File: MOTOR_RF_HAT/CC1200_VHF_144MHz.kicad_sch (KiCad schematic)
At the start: 41 parts, among them J1 SMA, U1 CC1200RHBR, Y1 40MHz

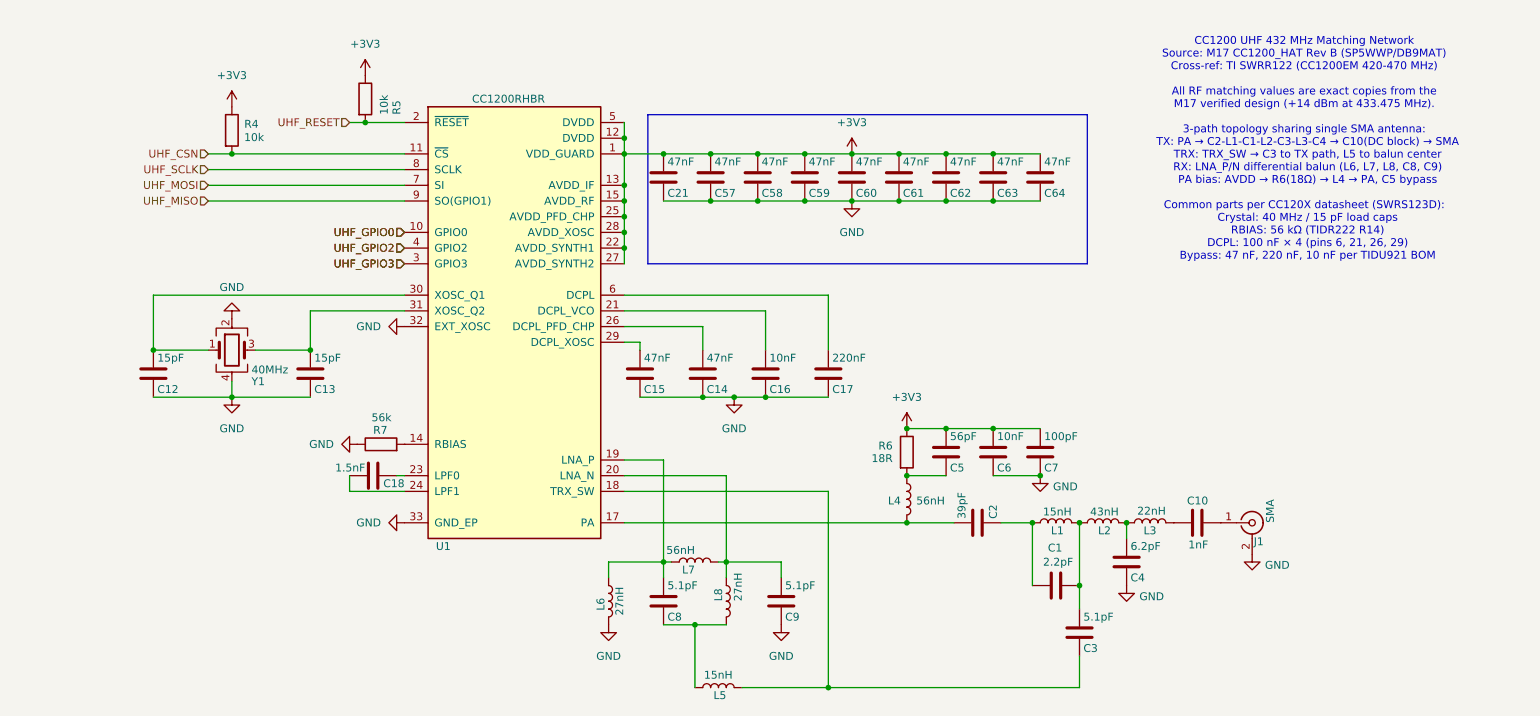
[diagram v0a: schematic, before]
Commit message: MOTOR_RF_HAT: port full RF_HAT project with all libs localized
Copied complete RF_HAT_out KiCad project (schematic + PCB layout +
4 hierarchical sub-sheets) as the base for the combined board.

Changes from original RF_HAT:
- Renamed RF_HAT → MOTOR_RF_HAT in all project/schematic references
- Imported LMR51420YDDCR + XRTC303020D4R7MBCA symbols from personal
  lib into project-local components.kicad_sym
- Copied corresponding footprints + 3D models (SOT-23-6, inductor)
  into components.pretty/ and components.3dshapes/
- Fixed all lib: → components: references in schematics and PCB
- Removed reference/ directory (schematics are now live sub-sheets)
- ERC: 20 violations (19 pre-existing from RF_HAT + 1 from rename)
- Zero external library dependencies — fully self-contained

Ready to add motor driver (A4950E), encoder, and IMU (ADXL345)
sub-sheets. Existing CC1200 UHF/VHF, Pi header, Pico, power,
NeoPixel, and buzzer circuits carry over unchanged.

Co-Authored-By: Claude Opus 4.6 (1M context) <noreply@anthropic.com>
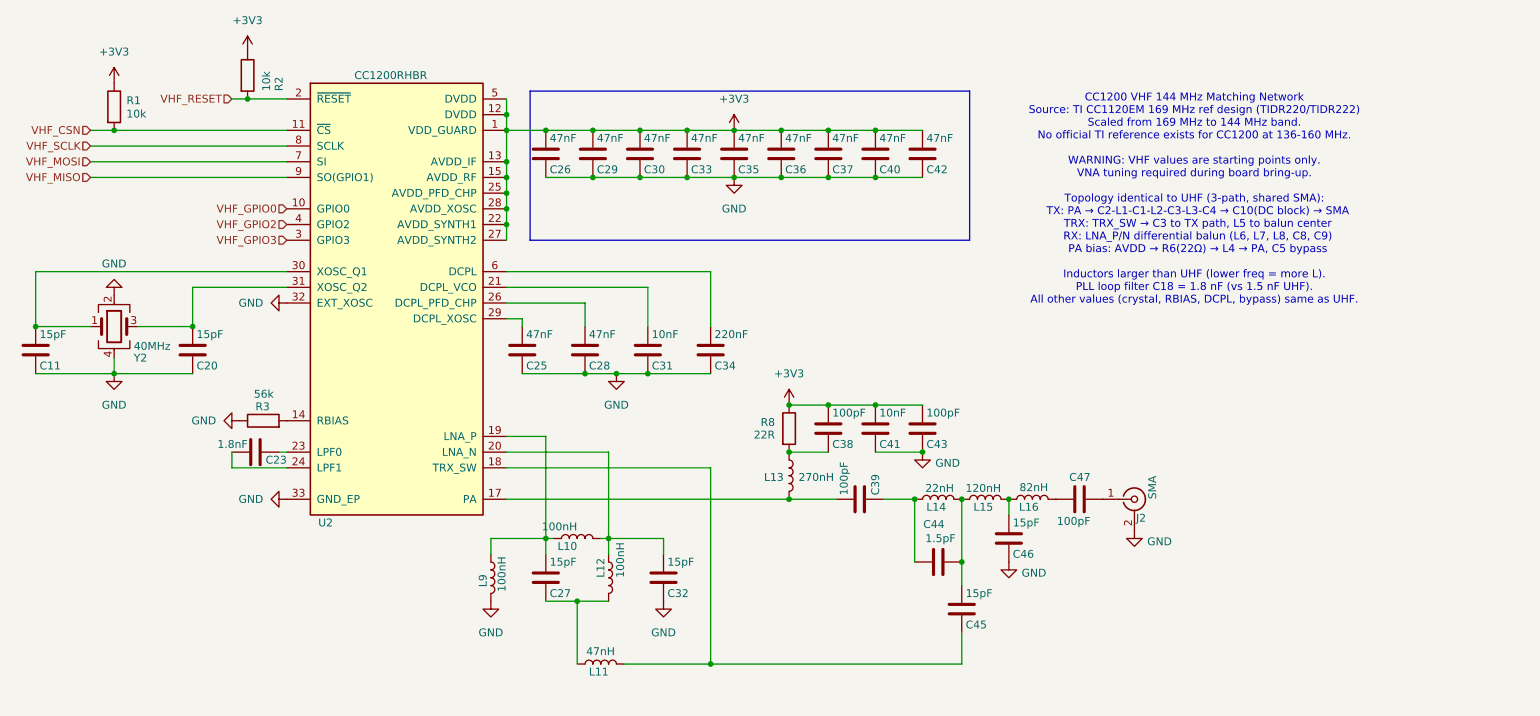
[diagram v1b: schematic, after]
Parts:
- removed C1: 2.2pF, Capacitor_SMD:C_0603_1608Metric, symbol Device:C
- removed C10: 1nF, Capacitor_SMD:C_0603_1608Metric, symbol Device:C
- removed C12, C13: 15pF, Capacitor_SMD:C_0603_1608Metric, symbol Device:C
- removed C14, C15, C21, C57, C58, C59, C60, C61, C62, C63, C64: 47nF, Capacitor_SMD:C_0603_1608Metric, symbol Device:C
- removed C16, C6: 10nF, Capacitor_SMD:C_0603_1608Metric, symbol Device:C
- removed C17: 220nF, Capacitor_SMD:C_0603_1608Metric, symbol Device:C
- removed C18: 1.5nF, Capacitor_SMD:C_0603_1608Metric, symbol Device:C
- removed C2: 39pF, Capacitor_SMD:C_0603_1608Metric, symbol Device:C
- removed C3, C8, C9: 5.1pF, Capacitor_SMD:C_0603_1608Metric, symbol Device:C
- removed C4: 6.2pF, Capacitor_SMD:C_0603_1608Metric, symbol Device:C
- removed C5: 56pF, Capacitor_SMD:C_0603_1608Metric, symbol Device:C
- removed C7: 100pF, Capacitor_SMD:C_0603_1608Metric, symbol Device:C
- removed J1: SMA, Connector_Coaxial:SMA_Amphenol_132289_EdgeMount, symbol Connector:Conn_Coaxial
- removed L1, L5: 15nH, Inductor_SMD:L_0603_1608Metric, symbol Device:L
- removed L2: 43nH, Inductor_SMD:L_0603_1608Metric, symbol Device:L
- removed L3: 22nH, Inductor_SMD:L_0603_1608Metric, symbol Device:L
- removed L4, L7: 56nH, Inductor_SMD:L_0603_1608Metric, symbol Device:L
- removed L6, L8: 27nH, Inductor_SMD:L_0603_1608Metric, symbol Device:L
- removed R4, R5: 10k, Resistor_SMD:R_0603_1608Metric, symbol Device:R
- removed R6: 18R, Resistor_SMD:R_0603_1608Metric, symbol Device:R
- removed R7: 56k, Resistor_SMD:R_0603_1608Metric, symbol Device:R
- removed U1: CC1200RHBR, Package_DFN_QFN:QFN-32-1EP_5x5mm_P0.5mm_EP3.45x3.45mm, symbol RF:CC1200
- removed Y1: 40MHz, Crystal:Crystal_SMD_3225-4Pin_3.2x2.5mm, symbol Device:Crystal_GND24
- added C11, C20, C27, C32, C45, C46: 15pF, Capacitor_SMD:C_0603_1608Metric, symbol Device:C
- added C23: 1.8nF, Capacitor_SMD:C_0603_1608Metric, symbol Device:C
- added C25, C26, C28, C29, C30, C33, C35, C36, C37, C40, C42: 47nF, Capacitor_SMD:C_0603_1608Metric, symbol Device:C
- added C31, C41: 10nF, Capacitor_SMD:C_0603_1608Metric, symbol Device:C
- added C34: 220nF, Capacitor_SMD:C_0603_1608Metric, symbol Device:C
- added C38, C39, C43, C47: 100pF, Capacitor_SMD:C_0603_1608Metric, symbol Device:C
- added C44: 1.5pF, Capacitor_SMD:C_0603_1608Metric, symbol Device:C
- added J2: SMA, Connector_Coaxial:SMA_Amphenol_132289_EdgeMount, symbol Connector:Conn_Coaxial
- added L10, L12, L9: 100nH, Inductor_SMD:L_0603_1608Metric, symbol Device:L
- added L11: 47nH, Inductor_SMD:L_0603_1608Metric, symbol Device:L
- added L13: 270nH, Inductor_SMD:L_0603_1608Metric, symbol Device:L
- added L14: 22nH, Inductor_SMD:L_0603_1608Metric, symbol Device:L
- added L15: 120nH, Inductor_SMD:L_0603_1608Metric, symbol Device:L
- added L16: 82nH, Inductor_SMD:L_0603_1608Metric, symbol Device:L
- added R1, R2: 10k, Resistor_SMD:R_0603_1608Metric, symbol Device:R
- added R3: 56k, Resistor_SMD:R_0603_1608Metric, symbol Device:R
- added R8: 22R, Resistor_SMD:R_0603_1608Metric, symbol Device:R
- added U2: CC1200RHBR, Package_DFN_QFN:QFN-32-1EP_5x5mm_P0.5mm_EP3.45x3.45mm, symbol RF:CC1200
- added Y2: 40MHz, Crystal:Crystal_SMD_3225-4Pin_3.2x2.5mm, symbol Device:Crystal_GND24
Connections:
- net +3V3: now also C26.1, C29.1, C30.1, C33.1, C35.1, C36.1, C37.1, C38.1, C40.1, C41.1, C42.1, C43.1, R1.1, R2.1, R8.1, U2.1 (VDD_GUARD), U2.12 (DVDD), U2.13 (AVDD_IF), U2.15 (AVDD_RF), U2.22 (AVDD_SYNTH1), U2.25 (AVDD_PFD_CHP), U2.27 (AVDD_SYNTH2), U2.28 (AVDD_XOSC), U2.5 (DVDD)
- net GND: now also C11.2, C20.2, C25.2, C26.2, C28.2, C29.2, C30.2, C31.2, C32.2, C33.2, C34.2, C35.2, C36.2, C37.2, C40.2, C41.2, C42.2, C43.2, C46.2, J2.2 (Ext), L9.2, R3.1, U2.32 (EXT_XOSC), U2.33 (GND_EP), Y2.2, Y2.4
- new net: C47.2, J2.1 (In)
- new net: C20.1, U2.31 (XOSC_Q2), Y2.3
- new net: C11.1, U2.30 (XOSC_Q1), Y2.1
- new net: C38.2, L13.1, R8.2
- new net: C28.1, U2.26 (DCPL_PFD_CHP)
- new net: C44.2, C45.1, L14.2, L15.1
- new net: C45.2, L11.2, U2.18 (TRX_SW)
- new net: R3.2, U2.14 (RBIAS)
- new net: C25.1, U2.29 (DCPL_XOSC)
- new net: C27.1, L10.1, L9.1, U2.19 (LNA_P)
- new net: C32.1, L10.2, L12.1, U2.20 (LNA_N)
- new net: C47.1, L16.2
- new net: C39.2, C44.1, L14.1
- new net: C34.1, U2.6 (DCPL)
- new net: C23.1, U2.24 (LPF1)
- new net: C23.2, U2.23 (LPF0)
- new net: C39.1, L13.2, U2.17 (PA)
- new net: C31.1, U2.21 (DCPL_VCO)
- new net: C27.2, L11.1, L12.2
- new net: C46.1, L15.2, L16.1
- new net VHF_CSN: R1.2, U2.11 (~{CS})
- new net VHF_GPIO0: U2.10 (GPIO0)
- new net VHF_GPIO2: U2.4 (GPIO2)
- new net VHF_GPIO3: U2.3 (GPIO3)
- new net VHF_MISO: U2.9 (SO(GPIO1))
- new net VHF_MOSI: U2.7 (SI)
- new net VHF_RESET: R2.2, U2.2 (~{RESET})
- new net VHF_SCLK: U2.8 (SCLK)
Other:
- note added: "CC1200 VHF 144 MHz Matching Network Source: TI CC1120EM 169 MHz ref design (TIDR220/TIDR222) Scaled from 169 MHz to 144 MHz band. No official TI reference exists for CC1200 at 136-160 MHz. WARNING: VHF values are starting points only. VNA tuning required during board bring-up. Topology identical to UHF (3-path, shared SMA): TX: PA → C2-L1-C1-L2-C3-L3-C4 → C10(DC block) → SMA TRX: TRX_SW → C3 to T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"
- note removed: "CC1200 UHF 432 MHz Matching Network Source: M17 CC1200_HAT Rev B (SP5WWP/DB9MAT) Cross-ref: TI SWRR122 (CC1200EM 420-470 MHz) All RF matching values are exact copies from the M17 verified design (+14 dBm at 433.475 MHz). 3-path topology sharing single SMA antenna: TX: PA → C2-L1-C1-L2-C3-L3-C4 → C10(DC block) → SMA TRX: TRX_SW → C3 to TX path, L5 to balun center RX: LNA_P/N differential balun (L6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"
- title: RF_HAT -> MOTOR_RF_HAT

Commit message: MOTOR_RF_HAT: add TestPoint lib alias to fix persistent smallpad errors
KiCad's lib_symbols cache keeps reverting footprint refs to
TestPoint:smallpad on save. Added TestPoint as a footprint library
alias pointing to components.pretty so both TestPoint:smallpad and
components:smallpad resolve to the same local footprint.

Co-Authored-By: Claude Opus 4.6 (1M context) <noreply@anthropic.com>
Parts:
- renumbered C20 to C10, C23 to C11, C25 to C14, C26 to C15, C27 to C16, C28 to C17, C29 to C18, C30 to C19, C31 to C21, C32 to C23, C33 to C25, C34 to C28, C35 to C29, C36 to C32, C37 to C35, C38 to C37, C42 to C43, C43 to C44, C44 to C45, C45 to C48, C46 to C52, C47 to C56, C11 to C8, J2 to J4, L13 to L10, L14 to L12, L15 to L13, L16 to L14, L9 to L2, L10 to L3, L11 to L4, L12 to L5, R1 to R3, R2 to R5, R3 to R6, R8 to R9, U2 to U3, Y2 to Y1

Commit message: MOTOR_RF_HAT: 0805→0603 passives, encoder caps 100nF→100pF
- Changed all capacitor and resistor footprints from 0805 to 0603
  across all schematic sheets (CC1200 UHF/VHF, root, azimuth,
  elevation, encoders)
- Fixed encoder RC filter caps C68-C71 from 100nF to 100pF
  (fc = 15.9 MHz, transparent to 35 kHz encoder signal)

Co-Authored-By: Claude Opus 4.6 (1M context) <noreply@anthropic.com>
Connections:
- net VHF_GPIO0: no longer names the net of U3.10 (GPIO0)
- net VHF_GPIO2: no longer names the net of U3.4 (GPIO2)
- net VHF_GPIO3: no longer names the net of U3.3 (GPIO3)
- no-connect marks 0 -> 3
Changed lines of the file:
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@@
 		(color 0 0 0 0)
+	)
+	(no_connect
+		(at 80.01 71.12)
+	)
+	(no_connect
+		(at 80.01 68.58)
+	)
+	(no_connect
+		(at 80.01 66.04)
 	)
 	(wire
@@
 		(effects
 			(font
-				(size 1.27 1.27)
-			)
-			(justify right)
-		)
-	)
-	(hierarchical_label "VHF_GPIO0"
-		(shape input)
-		(at 80.01 66.04 180)
-		(effects
-			(font
-				(size 1.27 1.27)
-			)
-			(justify right)
-		)
-	)
-	(hierarchical_label "VHF_GPIO3"
-		(shape input)
-		(at 80.01 71.12 180)
-		(effects
-			(font
-				(size 1.27 1.27)
-			)
-			(justify right)
-		)
-	)
-	(hierarchical_label "VHF_GPIO2"
-		(shape input)
-		(at 80.01 68.58 180)
-		(effects
-			(font
